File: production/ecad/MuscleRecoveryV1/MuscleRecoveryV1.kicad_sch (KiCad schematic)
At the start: 0 parts

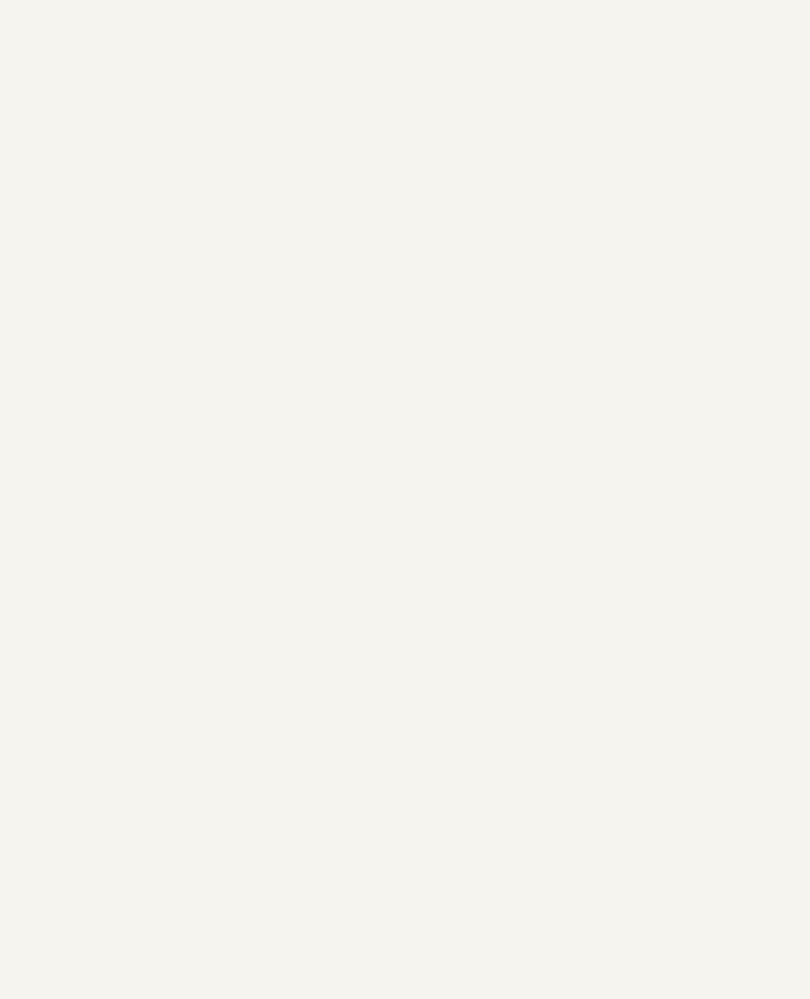
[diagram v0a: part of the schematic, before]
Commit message: Combined schematics together
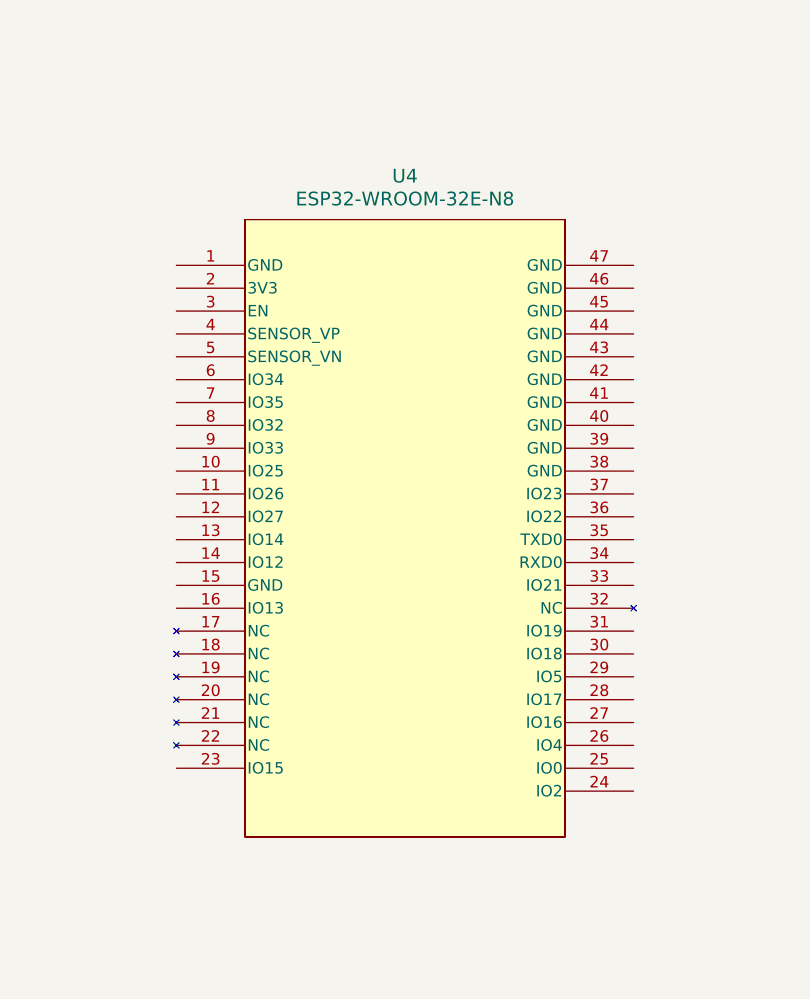
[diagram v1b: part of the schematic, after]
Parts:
- added U4: ESP32-WROOM-32E-N8, symbol ESP32-WROOM-32E-N8:ESP32-WROOM-32E-N8
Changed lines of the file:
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@@
     (company "Generate Product Development Studio")
+  )
+  (symbol (lib_id "ESP32-WROOM-32E-N8:ESP32-WROOM-32E-N8") (at 119.38 60.96 0) (unit 1)
+    (in_bom yes) (on_board yes) (dnp no) (fields_autoplaced)
+    (property "Reference" "U4" (at 144.78 51.054 0)
+      (effects (font (size 1.524 1.524)))
+    )
+    (property "Value" "ESP32-WROOM-32E-N8" (at 144.78 53.594 0)
+      (effects (font (size 1.524 1.524)))
+    )
+    (property "Footprint" "" (at 119.38 60.96 0)
+      (effects (font (size 1.27 1.27) italic) hide)
+    )
+    (property "Datasheet" "ESP32-WROOM-32E-N8" (at 119.38 60.96 0)
+      (effects (font (size 1.27 1.27) italic) hide)
+    )
+    (pin "1")
+    (pin "10")
+    (pin "11")
+    (pin "12")
+    (pin "13")
+    (pin "14")
+    (pin "15")
+    (pin "16")
+    (pin "17")
+    (pin "18")
+    (pin "19")
+    (pin "2")
+    (pin "20")
+    (pin "21")
+    (pin "22")
+    (pin "23")
+    (pin "24")
+    (pin "25")
+    (pin "26")
+    (pin "27")
+    (pin "28")
+    (pin "29")
+    (pin "3")
+    (pin "30")
+    (pin "31")
+    (pin "32")
+    (pin "33")
+    (pin "34")
+    (pin "35")
+    (pin "36")
+    (pin "37")
+    (pin "38")
+    (pin "39")
+    (pin "4")
+    (pin "40")
+    (pin "41")
+    (pin "42")
+    (pin "43")
+    (pin "44")
+    (pin "45")
+    (pin "46")
+    (pin "47")
+    (pin "5")
+    (pin "6")
+    (pin "7")
+    (pin "8")
+    (pin "9")
+    (instances
+      (project "MuscleRecoveryV1"
+        (path "/4e550305-79d2-4e4a-a502-817ebcc79f9a"
+          (reference "U4") (unit 1)
+        )
+      )
+      (project "Power For Muscle Recovery"
+        (path "/68ba6acb-d7b0-4091-ad4f-10769cda4f80"
+          (reference "U2") (unit 1)
+        )
+      )
+      (project "New Test"
+        (path "/ec7ffed6-1d2d-48f7-b073-d0a7d4b8c858"
+          (reference "U3") (unit 1)
+        )
+      )
+    )
   )
   (sheet (at 24.13 99.06) (size 63.5 52.07) (fields_autoplaced)

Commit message: Revert "Display commit 1"
This reverts commit 52e50f7827ccbfa861bea7a8a003d131d02fed89.
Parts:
- removed U4: ESP32-WROOM-32E-N8, symbol ESP32-WROOM-32E-N8:ESP32-WROOM-32E-N8
- added 3v31, GND1, MISO1, MOSI1, SCL, SDA1, SD_CS1, TFT_CLK1, TFT_CS1, TFT_DC1, TFT_RST1: TestPoint, symbol Connector:TestPoint
- added C12: 1uF, symbol Device:C_Small
- added C13: 10uF, symbol Device:C_Small
- added J3: Screw_Terminal_01x06, symbol Connector:Screw_Terminal_01x06
- added R30, R31: 4.7k, symbol Device:R
- added U6: ESP32-WROOM-32, RF_Module:ESP32-WROOM-32, symbol RF_Module:ESP32-WROOM-32
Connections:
- new net +3V3: 3v31.1, C12.1, C13.1, J3.6 (Pin_6), R30.1, R31.2, U6.2 (VDD)
- new net ALERT/READY: U6.10 (IO25)
- new net EN: U6.3 (EN)
- new net GND: C12.2, C13.2, GND1.1, J3.1 (Pin_1), U6.1 (GND), U6.15 (GND), U6.38 (GND), U6.39 (GND)
- new net IO0: U6.25 (IO0)
- new net IO32: J3.5 (Pin_5), U6.8 (IO32)
- new net IO33: J3.4 (Pin_4), U6.9 (IO33)
- new net IO34: J3.3 (Pin_3), U6.6 (IO34)
- new net IO35: J3.2 (Pin_2), U6.7 (IO35)
- new net MISO: MISO1.1, U6.31 (IO19)
- new net MOSI: MOSI1.1, U6.37 (IO23)
- new net RXD0: U6.34 (RXD0/IO3)
- new net SCL: R30.2, U6.33 (IO21)
- new net SDA: R31.1, SCL.1, SDA1.1, U6.36 (IO22)
- new net SD_CS: SD_CS1.1, U6.11 (IO26)
- new net TFT_CLK: TFT_CLK1.1, U6.30 (IO18)
- new net TFT_CS: TFT_CS1.1, U6.23 (IO15)
- new net TFT_DC: TFT_DC1.1, U6.24 (IO2)
- new net TFT_RST: TFT_RST1.1, U6.26 (IO4)
- new net TXD0: U6.35 (TXD0/IO1)
- no-connect marks 0 -> 15
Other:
- sheet Bootloading ports: added EN, IO0, RXD0, TXD0; removed none
- sheet Display ports: added MISO, MOSI, SD_CS, TFT_CLK, TFT_CS, TFT_DC, TFT_RST; removed none
- sheet EMG ports: added ALERT/LABEL, SCL, SDA; removed none
- sheet Power and Battery ports: added SCL, SDA; removed none

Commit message: Display push attempt
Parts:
- renumbered C13 to C12, C12 to C13, U6 to U4
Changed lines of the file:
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@@
   (symbol (lib_id "power:GND") (at 142.24 130.81 0) (unit 1)
     (in_bom yes) (on_board yes) (dnp no) (fields_autoplaced)
-    (property "Reference" "#PWR053" (at 142.24 137.16 0)
+    (property "Reference" "#PWR011" (at 142.24 137.16 0)
       (effects (font (size 1.27 1.27)) hide)
     )
@@
     (instances
       (project "MuscleRecoveryV1"
-        (path "/4e550305-79d2-4e4a-a502-817ebcc79f9a/648f095b-a230-48ff-8dbf-d0fbef398770"
-          (reference "#PWR053") (unit 1)
-        )
         (path "/4e550305-79d2-4e4a-a502-817ebcc79f9a"
           (reference "#PWR011") (unit 1)
@@
   (symbol (lib_id "Device:C_Small") (at 97.79 66.04 0) (unit 1)
     (in_bom yes) (on_board yes) (dnp no)
-    (property "Reference" "C13" (at 100.33 64.7763 0)
+    (property "Reference" "C12" (at 100.33 64.7763 0)
       (effects (font (size 1.27 1.27)) (justify left))
     )
@@
     (instances
       (project "MuscleRecoveryV1"
-        (path "/4e550305-79d2-4e4a-a502-817ebcc79f9a/648f095b-a230-48ff-8dbf-d0fbef398770"
-          (reference "C13") (unit 1)
-        )
         (path "/4e550305-79d2-4e4a-a502-817ebcc79f9a"
           (reference "C12") (unit 1)
@@
   (symbol (lib_id "Device:C_Small") (at 107.95 66.04 0) (unit 1)
     (in_bom yes) (on_board yes) (dnp no)
-    (property "Reference" "C12" (at 110.49 64.77 0)
+    (property "Reference" "C13" (at 110.49 64.77 0)
       (effects (font (size 1.27 1.27)) (justify left))
     )
@@
     (instances
       (project "MuscleRecoveryV1"
-        (path "/4e550305-79d2-4e4a-a502-817ebcc79f9a/648f095b-a230-48ff-8dbf-d0fbef398770"
-          (reference "C12") (unit 1)
-        )
         (path "/4e550305-79d2-4e4a-a502-817ebcc79f9a"
           (reference "C13") (unit 1)
@@
   (symbol (lib_id "power:GND") (at 97.79 71.755 0) (unit 1)
     (in_bom yes) (on_board yes) (dnp no) (fields_autoplaced)
-    (property "Reference" "#PWR052" (at 97.79 78.105 0)
+    (property "Reference" "#PWR046" (at 97.79 78.105 0)
       (effects (font (size 1.27 1.27)) hide)
     )
@@
     (instances
       (project "MuscleRecoveryV1"
-        (path "/4e550305-79d2-4e4a-a502-817ebcc79f9a/648f095b-a230-48ff-8dbf-d0fbef398770"
-          (reference "#PWR052") (unit 1)
-        )
         (path "/4e550305-79d2-4e4a-a502-817ebcc79f9a"
           (reference "#PWR046") (unit 1)
@@
   (symbol (lib_id "power:+3V3") (at 97.79 57.15 0) (unit 1)
     (in_bom yes) (on_board yes) (dnp no) (fields_autoplaced)
-    (property "Reference" "#PWR051" (at 97.79 60.96 0)
+    (property "Reference" "#PWR015" (at 97.79 60.96 0)
       (effects (font (size 1.27 1.27)) hide)
     )
@@
     (instances
       (project "MuscleRecoveryV1"
-        (path "/4e550305-79d2-4e4a-a502-817ebcc79f9a/648f095b-a230-48ff-8dbf-d0fbef398770"
-          (reference "#PWR051") (unit 1)
-        )
         (path "/4e550305-79d2-4e4a-a502-817ebcc79f9a"
           (reference "#PWR015") (unit 1)
@@
   (symbol (lib_id "power:GND") (at 107.95 71.755 0) (unit 1)
     (in_bom yes) (on_board yes) (dnp no) (fields_autoplaced)
-    (property "Reference" "#PWR053" (at 107.95 78.105 0)
+    (property "Reference" "#PWR047" (at 107.95 78.105 0)
       (effects (font (size 1.27 1.27)) hide)
     )
@@
     (instances
       (project "MuscleRecoveryV1"
-        (path "/4e550305-79d2-4e4a-a502-817ebcc79f9a/648f095b-a230-48ff-8dbf-d0fbef398770"
-          (reference "#PWR053") (unit 1)
-        )
         (path "/4e550305-79d2-4e4a-a502-817ebcc79f9a"
           (reference "#PWR047") (unit 1)
@@
   (symbol (lib_id "RF_Module:ESP32-WROOM-32") (at 142.24 91.44 0) (unit 1)
     (in_bom yes) (on_board yes) (dnp no)
-    (property "Reference" "U6" (at 128.905 53.975 0)
+    (property "Reference" "U4" (at 128.905 53.975 0)
       (effects (font (size 1.27 1.27)) (justify left))
     )
@@
     (instances
       (project "MuscleRecoveryV1"
-        (path "/4e550305-79d2-4e4a-a502-817ebcc79f9a/648f095b-a230-48ff-8dbf-d0fbef398770"
-          (reference "U6") (unit 1)
-        )
         (path "/4e550305-79d2-4e4a-a502-817ebcc79f9a"
           (reference "U4") (unit 1)

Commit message: Display and Push Button
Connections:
- net IO35: no longer U4.7 (IO35)
- net SD_CS: now also U4.13 (IO14); no longer U4.11 (IO26)
- net TFT_CLK: no longer U4.30 (IO18)
- net IO27: now reaches U4.12 (IO27)
- net LIT: now reaches U4.16 (IO13)
- new net SCK: U4.30 (IO18)
- new net START_BUTTON: U4.7 (IO35)
- no-connect marks 15 -> 13
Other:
- sheet Display ports: added LIT, SCK, START_BUTTON; removed TFT_CLK
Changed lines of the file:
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@@
   )
   (no_connect (at 127 101.6))
-  (no_connect (at 157.48 81.28))
   (no_connect (at 127 73.66))
   (no_connect (at 127 71.12))
   (no_connect (at 127 104.14))
+  (no_connect (at 157.48 86.36))
   (no_connect (at 157.48 73.66))
   (no_connect (at 127 93.98))
   (no_connect (at 127 99.06))
   (no_connect (at 157.48 88.9))
+  (no_connect (at 157.48 106.68))
   (no_connect (at 157.48 76.2))
   (no_connect (at 127 91.44))
-  (no_connect (at 157.48 86.36))
-  (no_connect (at 157.48 109.22))
-  (no_connect (at 157.48 78.74))
   (no_connect (at 127 96.52))
   (wire (pts (xy 86.36 36.83) (xy 95.25 36.83))
@@
     (stroke (width 0) (type default))
   )
-  (wire (pts (xy 157.48 106.68) (xy 165.1 106.68))
-    (stroke (width 0) (type default))
-  )
   (wire (pts (xy 107.95 63.5) (xy 107.95 60.96))
     (stroke (width 0) (type default))
@@
     (stroke (width 0) (type default))
   )
+  (wire (pts (xy 198.12 69.85) (xy 201.93 69.85))
+    (stroke (width 0) (type default))
+  )
   (wire (pts (xy 185.42 82.55) (xy 185.42 85.09))
     (stroke (width 0) (type default))
   )
+  (wire (pts (xy 157.48 71.12) (xy 165.1 71.12))
+    (stroke (width 0) (type default))
+  )
+  (wire (pts (xy 87.63 118.11) (xy 100.33 118.11))
+    (stroke (width 0) (type default))
+  )
+  (wire (pts (xy 21.59 173.99) (xy 38.1 173.99))
+    (stroke (width 0) (type default))
+  )
+  (wire (pts (xy 157.48 93.98) (xy 165.1 93.98))
+    (stroke (width 0) (type default))
+  )
+  (wire (pts (xy 157.48 78.74) (xy 165.1 78.74))
+    (stroke (width 0) (type default))
+  )
+  (wire (pts (xy 186.69 95.25) (xy 186.69 96.52))
+    (stroke (width 0) (type default))
+  )
+  (wire (pts (xy 157.48 81.28) (xy 165.1 81.28))
+    (stroke (width 0) (type default))
+  )
+  (wire (pts (xy 193.04 137.16) (xy 203.2 137.16))
+    (stroke (width 0) (type default))
+  )
+  (wire (pts (xy 123.19 64.77) (xy 127 64.77))
+    (stroke (width 0) (type default))
+  )
+  (wire (pts (xy 157.48 114.3) (xy 165.1 114.3))
+    (stroke (width 0) (type default))
+  )
+  (wire (pts (xy 186.69 85.09) (xy 186.69 87.63))
+    (stroke (width 0) (type default))
+  )
+  (wire (pts (xy 186.69 96.52) (xy 193.04 96.52))
+    (stroke (width 0) (type default))
+  )
+  (wire (pts (xy 115.57 188.595) (xy 125.095 188.595))
+    (stroke (width 0) (type default))
+  )
+  (wire (pts (xy 142.875 22.86) (xy 142.875 19.685))
+    (stroke (width 0) (type default))
+  )
+  (wire (pts (xy 182.88 99.06) (xy 193.04 99.06))
+    (stroke (width 0) (type default))
+  )
+  (wire (pts (xy 194.31 32.385) (xy 201.93 32.385))
+    (stroke (width 0) (type default))
+  )
+  (wire (pts (xy 133.985 27.94) (xy 140.97 27.94))
+    (stroke (width 0) (type default))
+  )
+  (wire (pts (xy 55.88 170.18) (xy 55.88 173.99))
+    (stroke (width 0) (type default))
+  )
   (wire (pts (xy 157.48 119.38) (xy 165.1 119.38))
     (stroke (width 0) (type default))
   )
-  (wire (pts (xy 157.48 71.12) (xy 165.1 71.12))
-    (stroke (width 0) (type default))
-  )
-  (wire (pts (xy 87.63 118.11) (xy 100.33 118.11))
-    (stroke (width 0) (type default))
-  )
-  (wire (pts (xy 21.59 173.99) (xy 38.1 173.99))
-    (stroke (width 0) (type default))
-  )
-  (wire (pts (xy 157.48 93.98) (xy 165.1 93.98))
-    (stroke (width 0) (type default))
-  )
-  (wire (pts (xy 186.69 95.25) (xy 186.69 96.52))
-    (stroke (width 0) (type default))
-  )
-  (wire (pts (xy 193.04 137.16) (xy 203.2 137.16))
-    (stroke (width 0) (type default))
-  )
-  (wire (pts (xy 123.19 64.77) (xy 127 64.77))
-    (stroke (width 0) (type default))
-  )
-  (wire (pts (xy 157.48 114.3) (xy 165.1 114.3))
-    (stroke (width 0) (type default))
-  )
-  (wire (pts (xy 186.69 85.09) (xy 186.69 87.63))
-    (stroke (width 0) (type default))
-  )
-  (wire (pts (xy 186.69 96.52) (xy 193.04 96.52))
-    (stroke (width 0) (type default))
-  )
-  (wire (pts (xy 115.57 188.595) (xy 125.095 188.595))
-    (stroke (width 0) (type default))
-  )
-  (wire (pts (xy 142.875 22.86) (xy 142.875 19.685))
-    (stroke (width 0) (type default))
-  )
-  (wire (pts (xy 182.88 99.06) (xy 193.04 99.06))
-    (stroke (width 0) (type default))
-  )
-  (wire (pts (xy 194.31 32.385) (xy 201.93 32.385))
-    (stroke (width 0) (type default))
-  )
-  (wire (pts (xy 133.985 27.94) (xy 140.97 27.94))
-    (stroke (width 0) (type default))
-  )
-  (wire (pts (xy 55.88 170.18) (xy 55.88 173.99))
-    (stroke (width 0) (type default))
-  )
   (wire (pts (xy 157.48 111.76) (xy 165.1 111.76))
     (stroke (width 0) (type default))
@@
     (stroke (width 0) (type default))
   )
+  (wire (pts (xy 157.48 109.22) (xy 165.1 109.22))
+    (stroke (width 0) (type default))
+  )
   (wire (pts (xy 115.57 184.785) (xy 115.57 188.595))
     (stroke (width 0) (type default))
@@
   )
   (wire (pts (xy 146.685 173.355) (xy 156.21 173.355))
+    (stroke (width 0) (type default))
+  )
+  (wire (pts (xy 194.31 64.77) (xy 201.93 64.77))
     (stroke (width 0) (type default))
   )
@@
     )
   )
+  (global_label "LIT" (shape output) (at 165.1 78.74 0) (fields_autoplaced)
+    (effects (font (size 1.27 1.27)) (justify left))
+    (property "Intersheetrefs" "${INTERSHEET_REFS}" (at 170.6857 78.74 0)
+      (effects (font (size 1.27 1.27)) (justify left) hide)
+    )
+  )
   (global_label "IO0" (shape input) (at 165.1 60.96 0) (fields_autoplaced)
     (effects (font (size 1.27 1.27)) (justify left))
@@
     )
   )
+  (global_label "START_BUTTON" (shape input) (at 198.12 69.85 180) (fields_autoplaced)
+    (effects (font (size 1.27 1.27)) (justify right))
+    (property "Intersheetrefs" "${INTERSHEET_REFS}" (at 181.4672 69.85 0)
+      (effects (font (size 1.27 1.27)) (justify right) hide)
+    )
+  )
   (global_label "MOSI" (shape input) (at 96.52 173.355 0) (fields_autoplaced)
     (effects (font (size 1.27 1.27)) (justify left))
@@
     )
   )
-  (global_label "TFT_CLK" (shape input) (at 194.31 43.18 180) (fields_autoplaced)
+  (global_label "SCK" (shape input) (at 194.31 43.18 180) (fields_autoplaced)
     (effects (font (size 1.27 1.27)) (justify right))
-    (property "Intersheetrefs" "${INTERSHEET_REFS}" (at 183.7653 43.18 0)
+    (property "Intersheetrefs" "${INTERSHEET_REFS}" (at 187.5753 43.18 0)
       (effects (font (size 1.27 1.27)) (justify right) hide)
     )
@@
     )
   )
+  (global_label "SD_CS" (shape output) (at 165.1 81.28 0) (fields_autoplaced)
+    (effects (font (size 1.27 1.27)) (justify left))
+    (property "Intersheetrefs" "${INTERSHEET_REFS}" (at 174.0118 81.28 0)
+      (effects (font (size 1.27 1.27)) (justify left) hide)
+    )
+  )
+  (global_label "LIT" (shape input) (at 194.31 64.77 180) (fields_autoplaced)
+    (effects (font (size 1.27 1.27)) (justify right))
+    (property "Intersheetrefs" "${INTERSHEET_REFS}" (at 188.7243 64.77 0)
+      (effects (font (size 1.27 1.27)) (justify right) hide)
+    )
+  )
   (global_label "TFT_RST" (shape input) (at 156.21 173.355 0) (fields_autoplaced)
     (effects (font (size 1.27 1.27)) (justify left))
@@
     )
   )
-  (global_label "SD_CS" (shape output) (at 165.1 106.68 0) (fields_autoplaced)
-    (effects (font (size 1.27 1.27)) (justify left))
-    (property "Intersheetrefs" "${INTERSHEET_REFS}" (at 174.0118 106.68 0)
-      (effects (font (size 1.27 1.27)) (justify left) hide)
-    )
-  )
   (global_label "SCL" (shape input) (at 100.33 118.11 0) (fields_autoplaced)
     (effects (font (size 1.27 1.27)) (justify left))
@@
     )
   )
-  (global_label "TFT_CLK" (shape output) (at 165.1 91.44 0) (fields_autoplaced)
-    (effects (font (size 1.27 1.27)) (justify left))
-    (property "Intersheetrefs" "${INTERSHEET_REFS}" (at 175.6447 91.44 0)
+  (global_label "SCK" (shape output) (at 165.1 91.44 0) (fields_autoplaced)
+    (effects (font (size 1.27 1.27)) (justify left))
+    (property "Intersheetrefs" "${INTERSHEET_REFS}" (at 171.8347 91.44 0)
       (effects (font (size 1.27 1.27)) (justify left) hide)
     )
@@
     )
   )
+  (global_label "START_BUTTON" (shape input) (at 165.1 119.38 0) (fields_autoplaced)
+    (effects (font (size 1.27 1.27)) (justify left))
+    (property "Intersheetrefs" "${INTERSHEET_REFS}" (at 181.7528 119.38 0)
+      (effects (font (size 1.27 1.27)) (justify left) hide)
+    )
+  )
   (global_label "MISO" (shape output) (at 194.31 38.1 180) (fields_autoplaced)
     (effects (font (size 1.27 1.27)) (justify right))
@@
     )
   )
+  (global_label "IO27" (shape bidirectional) (at 165.1 109.22 0) (fields_autoplaced)
+    (effects (font (size 1.27 1.27)) (justify left))
+    (property "Intersheetrefs" "${INTERSHEET_REFS}" (at 173.5508 109.22 0)
+      (effects (font (size 1.27 1.27)) (justify left) hide)
+    )
+  )
   (global_label "TFT_CS" (shape output) (at 165.1 83.82 0) (fields_autoplaced)
     (effects (font (size 1.27 1.27)) (justify left))
     (property "Intersheetrefs" "${INTERSHEET_REFS}" (at 174.5561 83.82 0)
-      (effects (font (size 1.27 1.27)) (justify left) hide)
-    )
-  )
-  (global_label "IO35" (shape bidirectional) (at 165.1 119.38 0) (fields_autoplaced)
-    (effects (font (size 1.27 1.27)) (justify left))
-    (property "Intersheetrefs" "${INTERSHEET_REFS}" (at 173.5508 119.38 0)
       (effects (font (size 1.27 1.27)) (justify left) hide)
     )
@@
       (effects (font (size 1.27 1.27)) (justify left))
     )
-    (pin "TFT_CLK" input (at 201.93 43.18 180)
-      (effects (font (size 1.27 1.27)) (justify left))
-    )
+    (pin "LIT" input (at 201.93 64.77 180)
+      (effects (font (size 1.27 1.27)) (justify left))
+    )
+    (pin "SCK" input (at 201.93 43.18 180)
+      (effects (font (size 1.27 1.27)) (justify left))
+    )
+    (pin "START_BUTTON" input (at 201.93 69.85 180)
+      (effects (font (size 1.27 1.27)) (justify left))
+    )
